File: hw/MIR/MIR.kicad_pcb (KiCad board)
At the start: 2 copper layers, 89.6 x 55 mm, 90 parts, among them J1 CONN_02X08, J10 CONN_01X01, J11 CONN_01X01, J12 CONN_01X01, J13 CONN_01X01, J14 CONN_01X01, J15 CONN_01X01, J16 CONN_01X01, J17 CONN_01X01, J18 CONN_01X01, J19 CONN_01X01, J2 CONN_02X08, J20 CONN_01X01, J21 CONN_01X01, J22 CONN_01X01, J23 CONN_01X01, J24 CONN_01X01, J25 CONN_01X01, J26 CONN_01X01, J27 CONN_01X01, J28 CONN_01X01, J29 CONN_01X01, J3 CONN_01X02, J30 CONN_01X01, J31 CONN_01X01, J32 CONN_01X01, J33 CONN_01X01, J34 CONN_01X01, J35 CONN_01X01, J36 CONN_01X01, J37 CONN_01X01, J38 CONN_01X01, J39 CONN_01X01, J40 CONN_01X01, J41 CONN_02X03, J42 CONN_01X15, J43 CONN_01X15, J44 USB_B_Mini, J9 CONN_01X01, SW1 SwitchPush, U1 ATmega328P-AU, U2 FT230XQ, Y1 16MHz

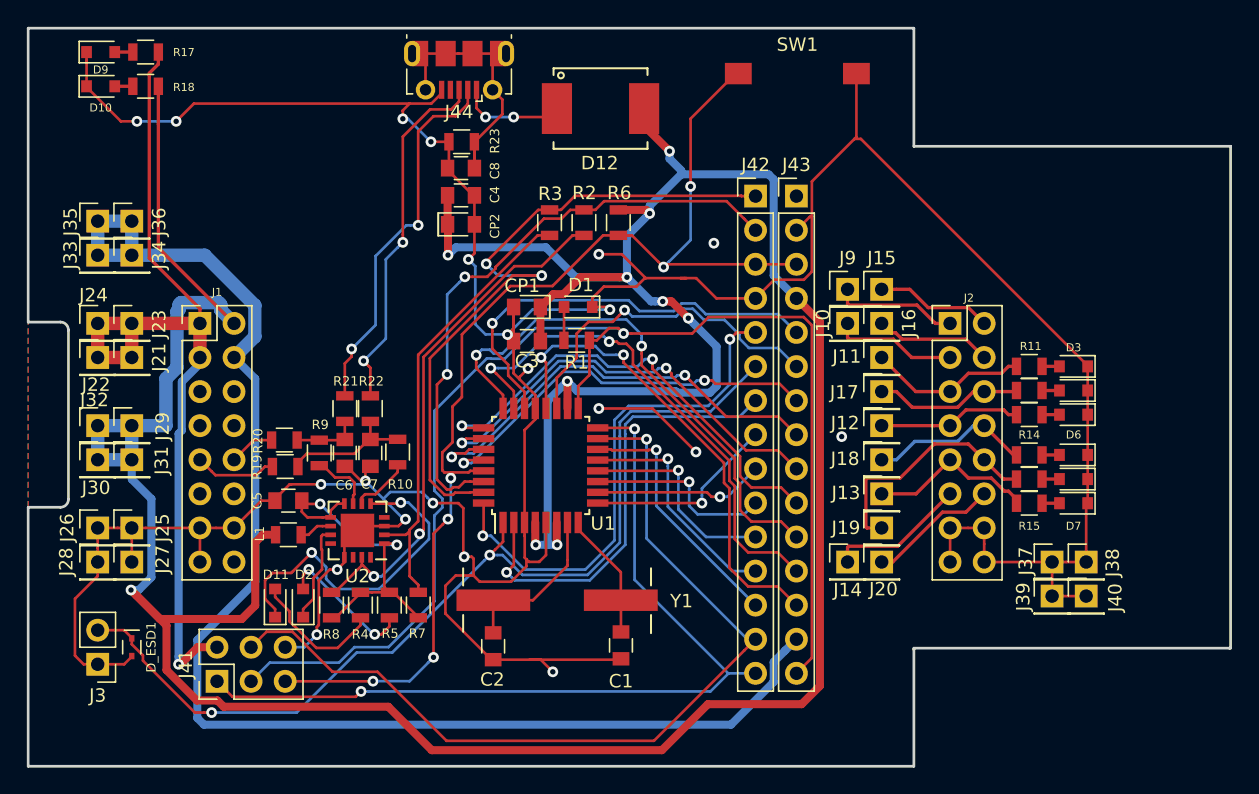
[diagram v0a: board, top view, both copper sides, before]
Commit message: Various fixes in schematics and PCB design
What has been done:

* Change Atmega328p footprint from TQFP to WQFN
* Replace FT230XQ with FT232RQ
* Adapt schematics to new FTDI chip
* Move capacitors further from XTAL
* Add load resistor for IR LED
* Add missing decoupling capacitors to some VDD pins
* Add cutout for NanoPi microUSB
* Remove unused USB connector
* Remove unused arduino connectors
* Remove not used (for MIR purposees) LEDs indicating state of STM GPIO
* Rename all files to MIR*
* Use only symbols from MIR libraries
* Rearrange texts on F.Mask layer
* Rearrange overlapping texts on F.Silk layer

Change-Id: Icd19173fda610c0574442d99b39109bb18bf1090
Signed-off-by: Katarzyna Gorska <k.gorska@samsung.com>
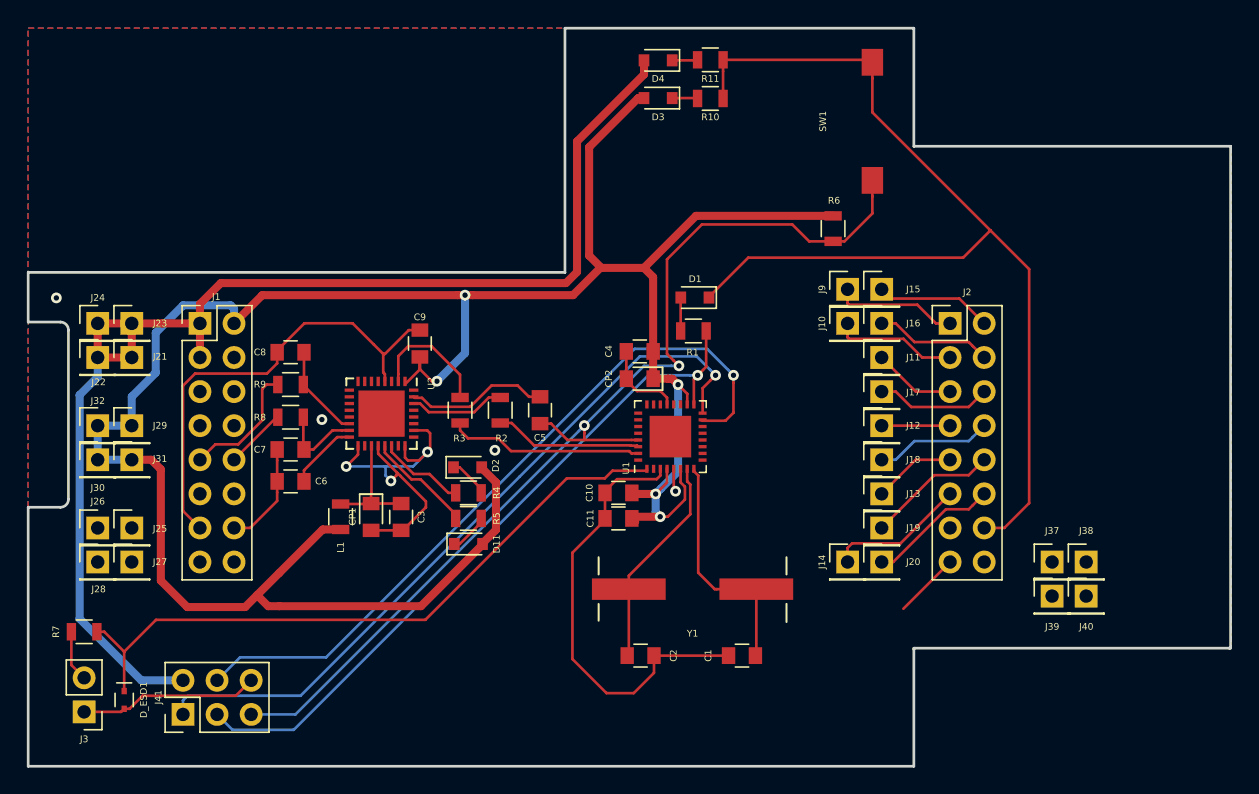
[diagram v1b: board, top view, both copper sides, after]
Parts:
- removed D10, D7: KPT-2012SGC, Diodes_SMD:D_0805
- removed D12: MBRS410L, Muxpi Addon:403AC
- removed D5, D8: OSB50805C1E, Diodes_SMD:D_0805
- removed D6, D9: KPT-2012EC, Diodes_SMD:D_0805
- removed J33, J34, J35, J36: CONN_01X01, Pin_Headers:Pin_Header_Straight_1x01_Pitch2.54mm
- removed J42, J43: CONN_01X15, Muxpi Addon:Pin_Header_Straight_1x15_Pitch2.54mm
- removed J44: USB_B_Mini, Muxpi Addon:USB_Micro-B_Molex-105017-0001
- removed R12, R13, R14, R15, R16, R17, R18: 330R, Resistors_SMD:R_0805
- removed R19, R20, R21, R22: 0, Muxpi Addon:R_0805
- removed R23: 10k, Muxpi Addon:R_0805
- added C10: 0.1uF, MIR:C_0805, F.Cu at (113.3, 169.2)
- added C11: 0.1uF, MIR:C_0805, F.Cu at (113.3, 171.1)
- added C9: 0.1uF, MIR:C_0805, F.Cu at (98.5, 158.1)
- C1, C2, C3, C4, C5: footprint Muxpi Addon:C_0805 -> MIR:C_0805
- C6: value 47pF/50V -> 0.1uF; footprint Muxpi Addon:C_0805 -> MIR:C_0805
- C7: value 47pF/50V -> 47pF; footprint Muxpi Addon:C_0805 -> MIR:C_0805
- C8: value 0.1uF -> 47pF; footprint Muxpi Addon:C_0805 -> MIR:C_0805
- CP1, CP2: footprint Muxpi Addon:C_T_0805 -> MIR:C_T_0805
- D1, D11, D3: footprint Diodes_SMD:D_0805 -> MIR:D_0805
- D2, D4: value KPT-2012SGC -> KPT-2012EC; footprint Diodes_SMD:D_0805 -> MIR:D_0805
- D_ESD1: footprint Muxpi Addon:SOD-523 -> MIR:SOD-523
- J1, J2: footprint Pin_Headers:Pin_Header_Straight_2x08_Pitch2.54mm -> MIR:Pin_Header_Straight_2x08_Pitch2.54mm
- J10, J11, J12, J13, J14, J15, J16, J17, J18, J19, J20, J21, J22, J23, J24, J25, J26, J27, J28, J29, J30, J31, J32, J37, J38, J39, J40, J9: footprint Pin_Headers:Pin_Header_Straight_1x01_Pitch2.54mm -> MIR:Pin_Header_Straight_1x01_Pitch2.54mm
- J3: footprint Pin_Headers:Pin_Header_Straight_1x02_Pitch2.54mm -> MIR:Pin_Header_Straight_1x02_Pitch2.54mm
- J41: footprint Muxpi Addon:Pin_Header_Straight_2x03_Pitch2.54mm -> MIR:Pin_Header_Straight_2x03_Pitch2.54mm
- L1, R1, R2, R3, R6, R9: footprint Muxpi Addon:R_0805 -> MIR:R_0805
- R10: value 27R -> 330R; footprint Muxpi Addon:R_0805 -> MIR:R_0805
- R11: footprint Resistors_SMD:R_0805 -> MIR:R_0805
- R4, R5: value 560R -> 330R; footprint Muxpi Addon:R_0805 -> MIR:R_0805
- R7: value 10k -> R; footprint Muxpi Addon:R_0805 -> MIR:R_0805
- R8: value 10k -> 27R; footprint Muxpi Addon:R_0805 -> MIR:R_0805
- SW1: footprint Muxpi Addon:DTSM-3 -> MIR:DTSM-3
- U1: value ATmega328P-AU -> ATmega328P-MU; footprint Muxpi Addon:TQFP-32_7x7mm_Pitch0.8mm -> MIR:WQFN-32-1EP_5x5mm_Pitch0.5mm
- U2: value FT230XQ -> FT232RQ; footprint Muxpi Addon:QFN-16-1EP_4x4mm_Pitch0.65mm -> MIR:QFN-32-1EP_5x5mm_Pitch0.5mm
- Y1: footprint Muxpi Addon:HC49USM -> MIR:HC49USM
- moved D4 39.5 mm to (116.2, 137.0)
- moved D3 36.9 mm to (116.2, 139.8)
- moved R10 35.2 mm to (120.1, 139.8), turned to 180 degrees
- moved R11 33.0 mm to (120.1, 137.0), turned to 180 degrees
- moved R7 25.0 mm to (73.5, 179.6), turned to 180 degrees
- moved C5 19.9 mm to (107.4, 163.1), turned to 270 degrees
- moved CP1 19.5 mm to (94.9, 171.0), turned to 270 degrees
- moved C8 18.7 mm to (88.9, 158.8), turned to 0 degrees
- moved C4 17.7 mm to (114.9, 158.7), turned to 180 degrees
- moved CP2 17.6 mm to (114.9, 160.7), turned to 180 degrees
- moved C3 16.1 mm to (97.1, 171.0), turned to 270 degrees
- moved R6 16.0 mm to (129.3, 149.5)
- moved D2 15.9 mm to (102.0, 167.3), turned to 0 degrees
- moved R3 15.5 mm to (101.5, 163.1), turned to 270 degrees
- moved R2 15.3 mm to (104.5, 163.1), turned to 270 degrees
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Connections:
- C3 pad 1: VDD -> /FT_VCC
- C5 pad 2: GND -> /RESET
- C6 pad 1: Net-(C6-Pad1) -> GND
- C6 pad 2: GND -> Net-(C6-Pad2)
- C8 pad 1: Net-(C8-Pad1) -> GND
- C8 pad 2: GND -> Net-(C8-Pad2)
- CP1 pad 1: VDD -> /FT_VCC
- D11 pad 2: Net-(D11-Pad2) -> VDD
- D2 pad 2: Net-(D2-Pad2) -> VDD
- D3 pad 1: GND -> Net-(D3-Pad1)
- D3 pad 2: Net-(D3-Pad2) -> VDD
- D4 pad 1: GND -> Net-(D4-Pad1)
- D4 pad 2: Net-(D4-Pad2) -> +5V
- J1 pad 11: /USB_A+ -> (no net)
- J1 pad 12: /USB_A- -> (no net)
- J1 pad 16: Net-(J1-Pad16) -> (no net)
- J1 pad 5: /SDA -> (no net)
- J1 pad 6: /SCL -> (no net)
- J1 pad 7: /PI_UART_TX -> (no net)
- J1 pad 8: /PI_UART_RX -> (no net)
- J3 pad 2: /D3 -> Net-(J3-Pad2)
- L1 pad 1: Net-(L1-Pad1) -> /FT_VCC
- R10 pad 1: Net-(C7-Pad1) -> GND
- R10 pad 2: Net-(R10-Pad2) -> Net-(D3-Pad1)
- R11 pad 1: /PI_GPIO_1 -> GND
- R11 pad 2: Net-(D3-Pad2) -> Net-(D4-Pad1)
- R4 pad 1: Net-(C5-Pad1) -> Net-(R4-Pad1)
- R4 pad 2: Net-(D11-Pad2) -> Net-(D2-Pad1)
- R5 pad 1: Net-(C5-Pad1) -> Net-(R5-Pad1)
- R5 pad 2: Net-(D2-Pad2) -> Net-(D11-Pad1)
- R7 pad 1: /TX -> /D3
- R7 pad 2: Net-(C5-Pad1) -> Net-(J3-Pad2)
- R8 pad 1: /RX -> /USB_B-
- R8 pad 2: Net-(C5-Pad1) -> Net-(C7-Pad1)
- R9 pad 1: Net-(C6-Pad1) -> /USB_B+
- R9 pad 2: Net-(R9-Pad2) -> Net-(C8-Pad2)
- U1 pad 10: /D6 -> (no net)
- U1 pad 11: /D7 -> (no net)
- U1 pad 12: /D8 -> (no net)
- U1 pad 13: /D9 -> (no net)
- U1 pad 14: /D10 -> (no net)
- U1 pad 19: /A6 -> (no net)
- U1 pad 2: /D4 -> (no net)
- U1 pad 20: /AREF -> (no net)
- U1 pad 22: /A7 -> (no net)
- U1 pad 23: /A0 -> (no net)
- U1 pad 24: /A1 -> (no net)
- U1 pad 25: /A2 -> (no net)
- U1 pad 26: /A3 -> (no net)
- U1 pad 27: /A4 -> (no net)
- U1 pad 28: /A5 -> (no net)
- U1 pad 32: /D2 -> (no net)
- U1 pad 9: /D5 -> (no net)
- U2 pad 1: Net-(C5-Pad1) -> VDD
- U2 pad 10: Net-(L1-Pad1) -> (no net)
- U2 pad 11: Net-(D2-Pad1) -> (no net)
- U2 pad 12: Net-(U2-Pad12) -> (no net)
- U2 pad 13: GND -> (no net)
- U2 pad 14: Net-(U2-Pad14) -> Net-(C8-Pad2)
- U2 pad 15: /RX -> Net-(C7-Pad1)
- U2 pad 16: Net-(U2-Pad16) -> Net-(C6-Pad2)
- U2 pad 3: GND -> (no net)
- U2 pad 4: Net-(U2-Pad4) -> GND
- U2 pad 5: Net-(D11-Pad1) -> (no net)
- U2 pad 6: Net-(R10-Pad2) -> (no net)
- U2 pad 7: Net-(R9-Pad2) -> (no net)
- U2 pad 8: Net-(C5-Pad1) -> (no net)
- U2 pad 9: Net-(C5-Pad1) -> (no net)
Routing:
- net +3V3: track 103.1 -> 0.00 mm
- net GND: track 307.9 -> 208.6 mm, vias 21 -> 7
- net VDD: track 272.2 -> 186.1 mm, vias 10 -> 5
- net /D13-SCK: track 97.4 -> 53.1 mm
- net /A1: track 40.1 -> 0.00 mm, vias 2 -> 0
- net /A0: track 38.5 -> 0.00 mm, vias 2 -> 0
- net /D2: track 38.4 -> 0.00 mm, vias 2 -> 0
- net /D1-TX: track 51.3 -> 14.5 mm, vias 2 -> 0
- net /AREF: track 36.0 -> 0.00 mm, vias 2 -> 0
- net /A2: track 35.1 -> 0.00 mm, vias 2 -> 0
- net /D0-RX: track 45.5 -> 11.0 mm, vias 2 -> 0
- net /D4: track 33.5 -> 0.00 mm, vias 1 -> 0
- net /A4: track 33.3 -> 0.00 mm, vias 2 -> 0
- net /A3: track 32.9 -> 0.00 mm, vias 2 -> 0
- net /A7: track 32.2 -> 0.00 mm, vias 1 -> 0
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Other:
- outline, holes or cut-outs redrawn
- board text removed: "SCL"
- board text removed: "SDA"
- board text removed: "UA+"
- board text removed: "UA-"
- board text removed: "UB+"
- board text removed: "UB-"
